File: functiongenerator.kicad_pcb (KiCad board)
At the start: 2 copper layers, 100 x 71 mm, 51 parts, among them J1 Amplitude, J2 offset, J3 Amplitude, J4 offset, J5 Conn_01x02_Socket, U1 LM6172, U2 LM6172, X1 ?2271611-, X2 ?2271611-

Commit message: pre release
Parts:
- added TP1: TestPoint_Small, TestPoint:TestPoint_Pad_D1.0mm, F.Cu at (139.7, 103.3)
- added TP2: TestPoint_Small, TestPoint:TestPoint_Pad_D1.0mm, F.Cu at (163.1, 85.2)
- added TP3: TestPoint_Small, TestPoint:TestPoint_Pad_D1.0mm, F.Cu at (194.3, 82.7)
- added TP4: TestPoint_Small, TestPoint:TestPoint_Pad_D1.0mm, F.Cu at (139.9, 127.5)
- added TP5: TestPoint_Small, TestPoint:TestPoint_Pad_D1.0mm, F.Cu at (162.7, 110.5)
- added TP6: TestPoint_Small, TestPoint:TestPoint_Pad_D1.0mm, F.Cu at (194.5, 123.5)
- C1, C3, C5: footprint functiongenerator:E2,5-7 -> Capacitor_THT:CP_Radial_D12.5mm_P5.00mm
- C2, C4, C6, C7, C8, C9: footprint functiongenerator:C025-030X050 -> Capacitor_THT:C_Disc_D3.0mm_W1.6mm_P2.50mm
- DC1: footprint functiongenerator:SIP3 -> Converter_DCDC:Converter_DCDC_TRACO_TSR-1_THT
- J5: footprint Connector_PinHeader_2.54mm:PinHeader_1x02_P2.54mm_Vertical -> Connector_PinSocket_2.54mm:PinSocket_1x02_P2.54mm_Vertical
- R1, R2, R3, R4, R5, R6, R7, R8: footprint functiongenerator:0204_7 -> Resistor_THT:R_Axial_DIN0204_L3.6mm_D1.6mm_P7.62mm_Horizontal
- SV1: renamed from SV2; footprint functiongenerator:FE07 -> Connector_PinSocket_2.54mm:PinSocket_1x07_P2.54mm_Vertical
- SV2: renamed from SV1; footprint functiongenerator:FE07 -> Connector_PinSocket_2.54mm:PinSocket_1x07_P2.54mm_Vertical
- SV4: footprint Connector_PinHeader_2.54mm:PinHeader_1x04_P2.54mm_Vertical -> Connector_PinSocket_2.54mm:PinSocket_1x04_P2.54mm_Vertical
- X1, X2: footprint functiongenerator:AMP_227161 -> Connector_Coaxial:LEMO-EPL.00.250.NTN
- moved R1 32.0 mm to (183.6, 89.2), turned to 180 degrees
- moved R6 31.5 mm to (183.4, 114.2), turned to 180 degrees
- moved J4 22.0 mm to (182.6, 129.1)
- moved R4 20.8 mm to (175.9, 92.5), turned to 0 degrees
- moved C15 20.3 mm to (162.9, 128.8), turned to 90 degrees
- moved R8 20.2 mm to (175.9, 117.7), turned to 0 degrees
- moved C5 20.2 mm to (158.2, 76.3), turned to 180 degrees
- moved C13 20.1 mm to (163.2, 105.2), turned to 90 degrees
- moved C1 19.5 mm to (178.4, 76.5), turned to 0 degrees
- moved J2 19.1 mm to (183.2, 102.5)
- moved C17 16.9 mm to (145.8, 127.6)
- moved C2 15.1 mm to (163.2, 99.7), turned to 0 degrees
- moved C16 14.8 mm to (146.9, 101.5)
- moved C4 14.4 mm to (170.8, 85.2), turned to 180 degrees
- moved C14 14.4 mm to (173.4, 105.6), turned to 180 degrees
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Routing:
- net /-12v: track 191.1 -> 154.1 mm
- net Net-(U1A-+): track 39.1 -> 16.2 mm
- net Net-(R10-Pad1): track 20.5 -> 40.7 mm
- net Net-(U2A-+): track 38.1 -> 18.4 mm
- net Net-(R13-Pad1): track 24.1 -> 37.9 mm
- net Net-(J3-Pin_2): track 27.1 -> 14.6 mm
- net /+12v: track 104.8 -> 117.1 mm
- net Net-(J1-Pin_2): track 26.0 -> 14.0 mm
- net Net-(J3-Pin_1): track 17.7 -> 29.6 mm
- net Net-(R8-Pad1): track 44.0 -> 32.6 mm
- net Net-(J1-Pin_1): track 18.0 -> 29.0 mm
- net Net-(R4-Pad1): track 43.2 -> 32.6 mm
- net Net-(C16-Pad2): track 14.1 -> 21.2 mm
- net Net-(U2B--): track 23.7 -> 17.2 mm
- net Net-(C17-Pad2): track 15.8 -> 22.0 mm
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
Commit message: optimized pcb layout
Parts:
- C1: value ~ -> 470uF
- C17: renamed from C3; value ~ -> 10uF
- C2: renamed from C5; value ~ -> 470uF
- C7: renamed from C16; value 2.2uF -> 10uF
- C8: renamed from C17; value 2.2uF -> 10uF
- R1: renamed from R2; value 33 -> 330
- R2: renamed from R3; value 33 -> 330
- RV1: value R_Potentiometer_Trim -> 2k
- SV3: renamed from SV1; value FE07-1 -> Conn_01x07_Socket
- X1: value ?2271611- -> CON1; footprint Connector_Coaxial:LEMO-EPL.00.250.NTN -> BNC:LINX_CONBNC002
- X2: value ?2271611- -> CON2; footprint Connector_Coaxial:LEMO-EPL.00.250.NTN -> BNC:LINX_CONBNC002
- moved TP6 17.0 mm to (183.7, 110.4)
- moved TP4 14.1 mm to (176.7, 110.3)
- moved TP5 10.9 mm to (183.9, 86.0)
- moved RV1 8.96 mm to (146.7, 93.2), turned to -90 degrees
- moved RV2 7.65 mm to (146.2, 118.9), turned to -90 degrees
- moved R8 7.45 mm to (176.0, 114.2), turned to 0 degrees
- moved J4 5.26 mm to (177.9, 102.8), turned to 0 degrees
- moved C2 4.95 mm to (153.3, 76.3), turned to 0 degrees
- moved J5 4.65 mm to (177.9, 129.0), turned to 0 degrees
- moved C17 3.85 mm to (129.6, 74.3)
- moved C15 3.36 mm to (170.0, 105.8)
- moved X1 2.16 mm to (192.6, 92.0), turned to 90 degrees
- moved X2 1.90 mm to (192.4, 115.7), turned to 90 degrees
- moved C1 0.63 mm to (179.0, 76.5)
- moved R12 0.07 mm to (176.0, 117.7)
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- renumbered C2 to C10, C12 to C11, C13 to C12, C6 to C13, C7 to C14, C14 to C15, C15 to C16, C10 to C3, C8 to C4, C9 to C5, C11 to C6, C4 to C9, J5 to J1, J1 to J2, J2 to J4, J4 to J5, R4 to R10, R7 to R11, R8 to R12, R9 to R13, R11 to R3, R10 to R4, R12 to R5, R13 to R6, R1 to R7, R6 to R8, R5 to R9, SV3 to SV1, SV4 to SV2, SV2 to SV4, TP4 to TP2, TP2 to TP3, TP5 to TP4, TP3 to TP5
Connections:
- C1 pad 1: (no net) -> /+12v
- C1 pad 2: (no net) -> GND
- C17 pad 1: (no net) -> /+5v
- C17 pad 2: (no net) -> GND
- C2 pad 1: (no net) -> GND
- C2 pad 2: (no net) -> /-12v
- R8 pad 1: Net-(U2B--) -> Net-(J3-Pin_1)
- R8 pad 2: Net-(J3-Pin_1) -> Net-(U2B--)
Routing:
- net /+12v: track 117.1 -> 132.7 mm
- net /-12v: track 154.1 -> 139.8 mm
- net Net-(R10-Pad1): track 32.6 -> 24.7 mm
- net Net-(R12-Pad1): track 32.6 -> 24.7 mm
- net Net-(C8-Pad2): track 22.0 -> 18.4 mm
- net Net-(C7-Pad2): track 21.2 -> 19.0 mm
- net Net-(J3-Pin_1): track 29.6 -> 31.2 mm
- net /+5v: track 85.3 -> 84.6 mm
- net Net-(U2A-+): track 18.4 -> 19.1 mm
- net Net-(U1A-+): track 16.2 -> 16.7 mm

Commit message: optimizing pcb design
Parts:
- R1, R11, R2, R9: footprint Resistor_THT:R_Axial_DIN0204_L3.6mm_D1.6mm_P7.62mm_Horizontal -> Resistor_THT:R_Axial_DIN0207_L6.3mm_D2.5mm_P7.62mm_Horizontal
- R10, R12, R7, R8: value 1000 -> 1k; footprint Resistor_THT:R_Axial_DIN0204_L3.6mm_D1.6mm_P7.62mm_Horizontal -> Resistor_THT:R_Axial_DIN0207_L6.3mm_D2.5mm_P7.62mm_Horizontal
- R13: value 390 -> 330
- R3, R4, R5, R6: footprint Resistor_THT:R_Axial_DIN0204_L3.6mm_D1.6mm_P5.08mm_Horizontal -> Resistor_THT:R_Axial_DIN0207_L6.3mm_D2.5mm_P7.62mm_Horizontal
- SV1: footprint TerminalBlock_Phoenix:TerminalBlock_Phoenix_PT-1,5-3-3.5-H_1x03_P3.50mm_Horizontal -> TerminalBlock_MetzConnect:TerminalBlock_MetzConnect_Type059_RT06303HBWC_1x03_P3.50mm_Horizontal
- SV4: value FE07-1 -> Conn_01x07_Socket
- moved TP6 17.5 mm to (191.6, 126.0)
- moved TP4 14.2 mm to (162.5, 109.7)
- moved TP5 9.02 mm to (191.7, 81.4)
- moved C15 5.02 mm to (173.5, 109.5), turned to 0 degrees
- moved C7 2.59 mm to (144.3, 101.5)
- moved R3 2.59 mm to (150.0, 101.5)
- moved R4 2.50 mm to (150.2, 105.8)
- moved C8 2.40 mm to (143.4, 127.6)
- moved R6 2.40 mm to (148.7, 132.4)
- moved R5 2.40 mm to (148.7, 127.5)
- moved X1 1.65 mm to (192.6, 90.4)
- moved R7 0.90 mm to (183.5, 88.3)
- moved C13 0.64 mm to (170.5, 110.1)
- moved R1 0.39 mm to (148.3, 97.5)
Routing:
- net Net-(R12-Pad1): track 24.7 -> 32.5 mm
- net Net-(R10-Pad1): track 24.7 -> 31.9 mm
- net /+12v: track 132.7 -> 126.9 mm
- net Net-(SV3-Pin_1): track 40.7 -> 38.1 mm
- net Net-(SV4-Pin_1): track 37.9 -> 35.8 mm
- net Net-(C7-Pad2): track 19.0 -> 17.9 mm
- net Net-(U1B--): track 16.5 -> 17.5 mm

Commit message: optimizing pcb design
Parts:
- added R2: 680, Resistor_THT:R_Axial_DIN0207_L6.3mm_D2.5mm_P7.62mm_Horizontal, F.Cu at (149.8, 83.3)
- added R4: 680, Resistor_THT:R_Axial_DIN0207_L6.3mm_D2.5mm_P7.62mm_Horizontal, F.Cu at (149.2, 109.2)
- R11: renamed from R9; value 500 -> 520
- R13: renamed from R11; value 500 -> 520
- R5: renamed from R3; value 18k -> 10k
- R7: renamed from R5; value 18k -> 10k
- RV2: value R_Potentiometer_Trim -> 2k
- renumbered R8 to R10, R10 to R12, R12 to R14, R13 to R15, R2 to R3, R4 to R6, R6 to R8, R7 to R9
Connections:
- RV1 pad 3: /-12v -> Net-(R2-Pad2)
- RV2 pad 3: /-12v -> Net-(R4-Pad2)
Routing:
- net /-12v: track 139.8 -> 130.7 mm
- net Net-(R2-Pad2): track 0.00 -> 8.26 mm
- net Net-(R4-Pad2): track 0.00 -> 8.08 mm

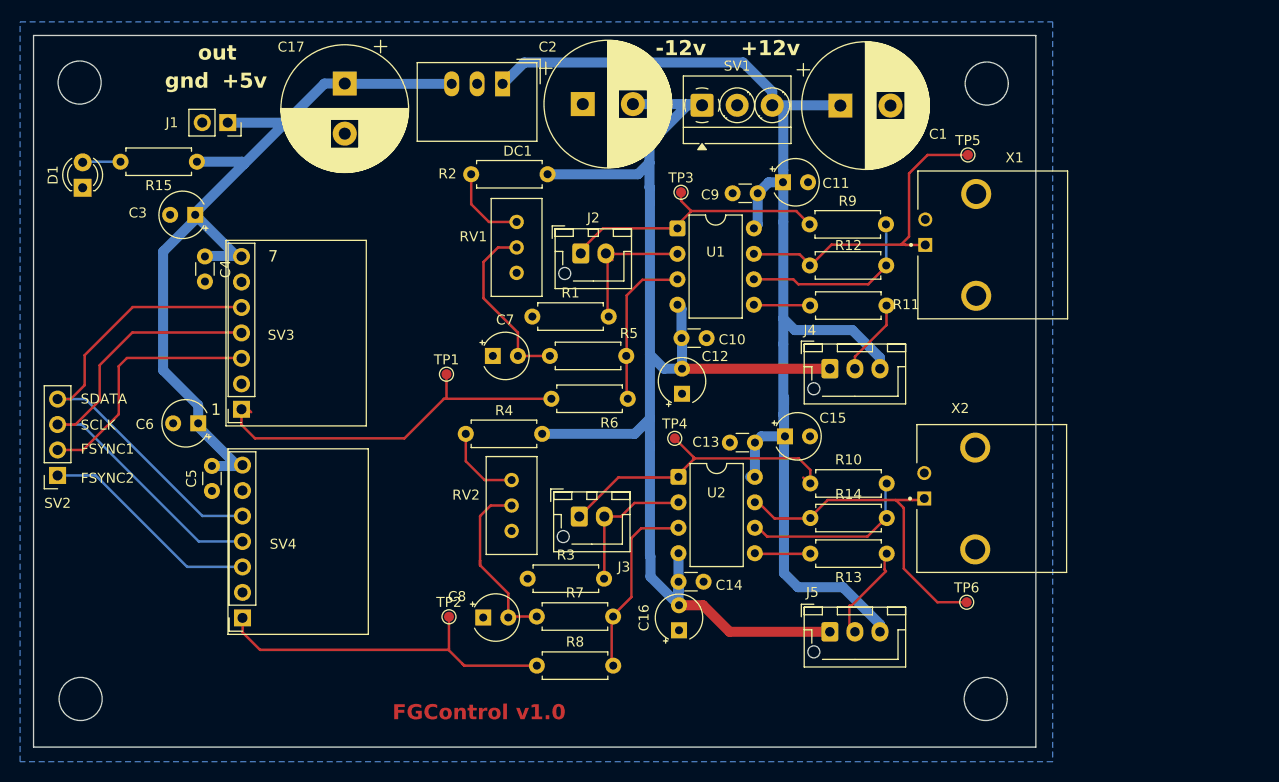
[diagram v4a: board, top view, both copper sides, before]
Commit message: added gnd to inout connector to reduce grounding loops
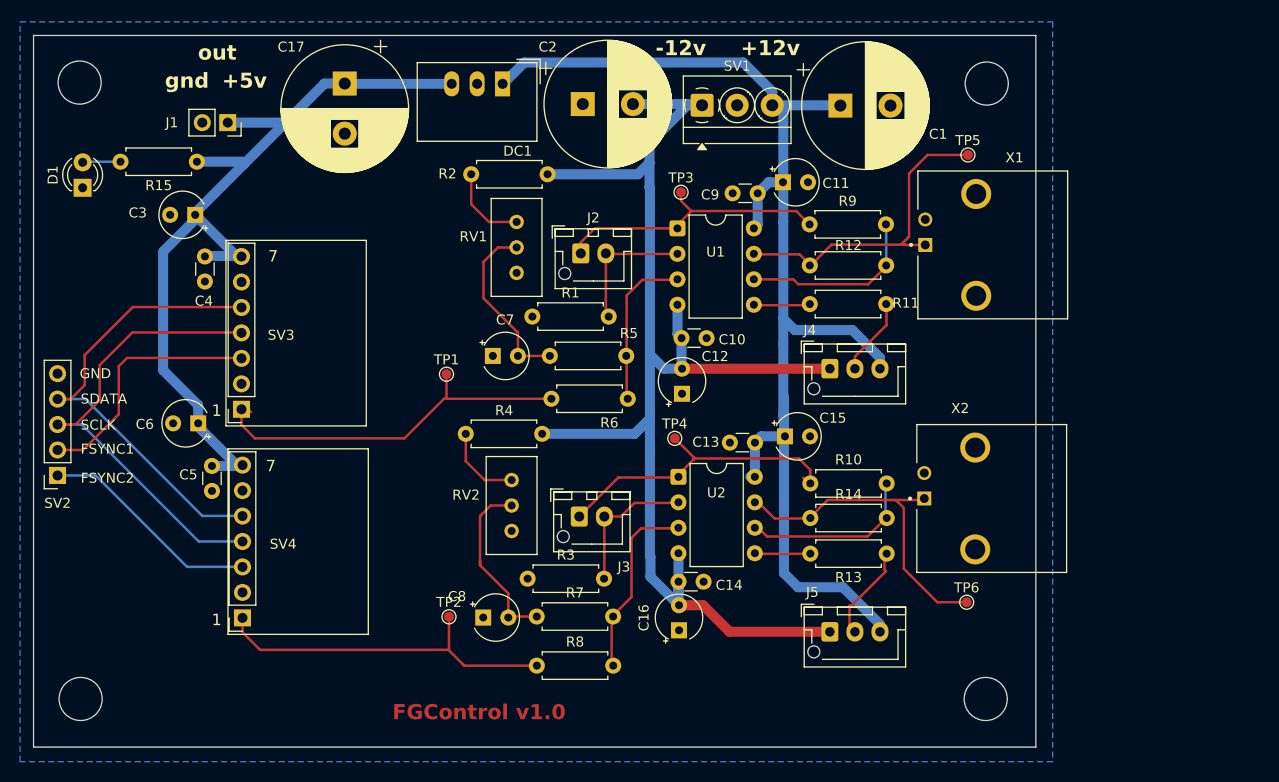
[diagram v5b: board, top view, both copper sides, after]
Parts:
- RV1, RV2: value 2k -> 500
- SV2: value Conn_01x04_Socket -> Conn_01x05_Socket; footprint Connector_PinSocket_2.54mm:PinSocket_1x04_P2.54mm_Vertical -> Connector_PinSocket_2.54mm:PinSocket_1x05_P2.54mm_Vertical
- moved R11 0.15 mm to (183.6, 96.3)
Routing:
- net Net-(J2-Pin_1): track 28.7 -> 30.2 mm
- net Net-(U1B--): track 17.5 -> 18.4 mm
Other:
- board text added: "GND"
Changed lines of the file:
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@@
 		(tags "C Disc series Radial pin pitch 2.50mm  diameter 3.0mm width 1.6mm Capacitor")
 		(property "Reference" "C5"
-			(at 1.25 -2.05 90)
+			(at 1.625 -2.35 180)
 			(layer "F.SilkS")
 			(effects
@@
 			(at 1.25 2.05 90)
 			(layer "F.Fab")
+			(hide yes)
 			(effects
 				(font
@@
 		(tags "C Disc series Radial pin pitch 2.50mm  diameter 3.0mm width 1.6mm Capacitor")
 		(property "Reference" "C4"
-			(at 1.25 -2.05 270)
+			(at 4.45 0.1 0)
 			(layer "F.SilkS")
 			(effects
@@
 			(at 1.25 2.05 270)
 			(layer "F.Fab")
+			(hide yes)
 			(effects
 				(font
@@
 			)
 		)
-		(property "Value" "2k"
+		(property "Value" "500"
 			(at -2.54 3.67 90)
 			(layer "F.Fab")
@@
 			)
 		)
-		(property "Value" "2k"
+		(property "Value" "500"
 			(at -2.54 3.67 90)
 			(layer "F.Fab")
@@
 		)
 	)
-	(footprint "Connector_PinSocket_2.54mm:PinSocket_1x04_P2.54mm_Vertical"
+	(footprint "Connector_PinSocket_2.54mm:PinSocket_1x05_P2.54mm_Vertical"
 		(layer "F.Cu")
 		(at 100.9 113.4 180)
-		(descr "Through hole straight socket strip, 1x04, 2.54mm pitch, single row (from Kicad 4.0.7), script generated")
-		(tags "Through hole socket strip THT 1x04 2.54mm single row")
+		(descr "Through hole straight socket strip, 1x05, 2.54mm pitch, single row (from Kicad 4.0.7), script generated")
+		(tags "Through hole socket strip THT 1x05 2.54mm single row")
 		(property "Reference" "SV2"
 			(at 0 -2.77 180)
@@
 			)
 		)
-		(property "Value" "Conn_01x04_Socket"
-			(at 0 10.39 180)
+		(property "Value" "Conn_01x05_Socket"
+			(at 0 12.93 180)
 			(layer "F.Fab")
 			(hide yes)
@@
 		(fp_line
 			(start 1.33 1.27)
-			(end 1.33 8.95)
+			(end 1.33 11.49)
 			(stroke
 				(width 0.12)
@@
 		)
 		(fp_line
-			(start -1.33 8.95)
-			(end 1.33 8.95)
+			(start -1.33 11.49)
+			(end 1.33 11.49)
 			(stroke
 				(width 0.12)
@@
 		(fp_line
 			(start -1.33 1.27)
-			(end -1.33 8.95)
+			(end -1.33 11.49)
 			(stroke
 				(width 0.12)
@@
 		)
 		(fp_line
-			(start 1.75 9.4)
-			(end -1.8 9.4)
+			(start 1.75 11.9)
+			(end -1.8 11.9)
 			(stroke
 				(width 0.05)
@@
 		(fp_line
 			(start 1.75 -1.8)
-			(end 1.75 9.4)
+			(end 1.75 11.9)
 			(stroke
 				(width 0.05)
@@
 		)
 		(fp_line
-			(start -1.8 9.4)
+			(start -1.8 11.9)
 			(end -1.8 -1.8)
 			(stroke
@@
 		)
 		(fp_line
-			(start 1.27 8.89)
-			(end -1.27 8.89)
+			(start 1.27 11.43)
+			(end -1.27 11.43)
 			(stroke
 				(width 0.1)
@@
 		(fp_line
 			(start 1.27 -0.635)
-			(end 1.27 8.89)
+			(end 1.27 11.43)
 			(stroke
 				(width 0.1)
@@
 		)
 		(fp_line
-			(start -1.27 8.89)
+			(start -1.27 11.43)
 			(end -1.27 -1.27)
 			(stroke
@@
 		)
 		(fp_text user "${REFERENCE}"
-			(at 0 3.81 270)
+			(at 0 5.08 270)
 			(layer "F.Fab")
 			(effects
@@
 			(pintype "passive")
 		)
+		(pad "5" thru_hole oval
+			(at 0 10.16 180)
+			(size 1.7 1.7)
+			(drill 1)
+			(layers "*.Cu" "*.Mask")
+			(remove_unused_layers no)
+			(net 1 "GND")
+			(pinfunction "Pin_5")
+			(pintype "passive")
+		)
 		(embedded_fonts no)
-		(model "${KICAD9_3DMODEL_DIR}/Connector_PinSocket_2.54mm.3dshapes/PinSocket_1x04_P2.54mm_Vertical.wrl"
+		(model "${KICAD9_3DMODEL_DIR}/Connector_PinSocket_2.54mm.3dshapes/PinSocket_1x05_P2.54mm_Vertical.wrl"
 			(offset
 				(xyz 0 0 0)
@@
 	(footprint "Resistor_THT:R_Axial_DIN0207_L6.3mm_D2.5mm_P7.62mm_Horizontal"
 		(layer "F.Cu")
-		(at 183.6 96.45 180)
+		(at 183.57 96.3 180)
 		(descr "Resistor, Axial_DIN0207 series, Axial, Horizontal, pin pitch=7.62mm, 0.25W = 1/4W, length*diameter=6.3*2.5mm^2, http://cdn-reichelt.de/documents/datenblatt/B400/1_4W%23YAG.pdf")
 		(tags "Resistor Axial_DIN0207 series Axial Horizontal pin pitch 7.62mm 0.25W = 1/4W length 6.3mm diameter 2.5mm")
@@
 		)
 	)
+	(gr_text "GND"
+		(at 103.1 103.825 0)
+		(layer "F.SilkS")
+		(effects
+			(font
+				(size 1 1)
+				(thickness 0.15)
+			)
+			(justify left bottom)
+		)
+	)
 	(gr_text "1"
-		(at 117.2 107.5 0)
+		(at 117.275 107.6 0)
 		(layer "F.SilkS")
 		(effects
@@
 		)
 	)
+	(gr_text "1"
+		(at 117.275 128.475 0)
+		(layer "F.SilkS")
+		(effects
+			(font
+				(size 1.143 1.143)
+				(thickness 0.127)
+			)
+			(justify right bottom)
+		)
+	)
 	(gr_text "out"
 		(at 114.9 72.1 0)
@@
 	)
 	(gr_text "7"
+		(at 122.675 113.125 0)
+		(layer "F.SilkS")
+		(effects
+			(font
+				(size 1.143 1.143)
+				(thickness 0.127)
+			)
+			(justify right bottom)
+		)
+	)
+	(gr_text "7"
 		(at 122.9 92.2 0)
 		(layer "F.SilkS")
@@
 	)
 	(segment
-		(start 183.57 89.25)
-		(end 183.57 92.36)
+		(start 183.57 92.36)
+		(end 183.57 88.375)
+		(width 0.25)
+		(layer "B.Cu")
+		(net 2)
+	)
+	(segment
+		(start 183.57 88.375)
+		(end 183.545 88.35)
 		(width 0.25)
 		(layer "B.Cu")
@@
 	)
 	(segment
-		(start 156.27 91.92)
-		(end 155.6 91.25)
+		(start 155.6 91.25)
+		(end 155.775 91.425)
 		(width 0.25)
 		(layer "F.Cu")
@@
 	)
 	(segment
-		(start 155.775 97.255)
-		(end 155.775 91.625)
+		(start 155.6 91.25)
+		(end 155.6 97.265)
 		(width 0.25)
 		(layer "F.Cu")
@@
 	)
 	(segment
-		(start 156.2 91.3)
-		(end 163.36 91.3)
+		(start 155.625 91.3)
+		(end 162.785 91.3)
 		(width 0.25)
 		(layer "F.Cu")
@@
 	)
 	(segment
-		(start 156.2 91.45)
-		(end 156.26 91.51)
+		(start 155.6 97.265)
+		(end 155.885 97.55)
 		(width 0.25)
 		(layer "F.Cu")
@@
 	)
 	(segment
-		(start 156.2 91.3)
-		(end 156.2 91.45)
+		(start 156.2 91.45)
+		(end 156.26 91.51)
 		(width 0.25)
 		(layer "F.Cu")
@@
 	)
 	(segment
-		(start 162.745 88.405)
-		(end 164.126 87.024)
+		(start 156.2 91.3)
+		(end 156.2 91.45)
 		(width 0.25)
 		(layer "F.Cu")
-		(net 10)
+		(net 9)
 	)
 	(segment
-		(start 153.7 90.35)
-		(end 153.7 90.45)
+		(start 154.5 88.75)
+		(end 162.745 88.75)
 		(width 0.25)
 		(layer "F.Cu")
@@
 	(segment
 		(start 153.1 91.25)
+		(end 153.1 90.15)
+		(width 0.25)
+		(layer "F.Cu")
+		(net 10)
+	)
+	(segment
+		(start 162.745 88.405)
+		(end 164.126 87.024)
+		(width 0.25)
+		(layer "F.Cu")
+		(net 10)
+	)
+	(segment
+		(start 153.1 91.25)
 		(end 153.1 91.05)
 		(width 0.25)
@@
 	)
 	(segment
-		(start 162.745 88.75)
-		(end 155.3 88.75)
-		(width 0.25)
-		(layer "F.Cu")
-		(net 10)
-	)
-	(segment
-		(start 155.3 88.75)
-		(end 153.7 90.35)
+		(start 153.1 90.15)
+		(end 154.5 88.75)
 		(width 0.25)
 		(layer "F.Cu")
@@
 	)
 	(segment
+		(start 163.15 102.7)
+		(end 163.2 102.75)
+		(width 1)
+		(layer "B.Cu")
+		(net 16)
+	)
+	(segment
 		(start 163.2 99.75)
 		(end 163.15 99.7)
@@
 	)
 	(segment
-		(start 163.15 99.7)
-		(end 163.15 96.775)
+		(start 162.745 96.37)
+		(end 162.745 99.295)
 		(width 1)
 		(layer "B.Cu")
@@
 	)
 	(segment
-		(start 163.2 102.75)
-		(end 163.2 99.75)
-		(width 1)
-		(layer "B.Cu")
-		(net 16)
-	)
-	(segment
 		(start 160 110.628856)
 		(end 160 121.44)
@@
 	)
 	(segment
+		(start 162.745 99.295)
+		(end 163.15 99.7)
+		(width 1)
+		(layer "B.Cu")
+		(net 16)
+	)
+	(segment
 		(start 165.1675 76.5)
 		(end 165.2 76.4675)
@@
 	)
 	(segment
-		(start 162.9 126.35)
-		(end 160.05 123.5)
+		(start 163.15 99.7)
+		(end 163.15 102.7)
 		(width 1)
 		(layer "B.Cu")
@@
 	)
 	(segment
-		(start 163.15 96.775)
-		(end 162.745 96.37)
+		(start 162.9 126.35)
+		(end 160.05 123.5)
 		(width 1)
 		(layer "B.Cu")
@@
 		(width 1)
 		(layer "B.Cu")
-		(net 17)
-	)
-	(segment
-		(start 111.428856 91.071262)
-		(end 111.500059 91.000059)
-		(width 1)
-		(layer "B.Cu")
